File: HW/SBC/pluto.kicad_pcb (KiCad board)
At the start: 2 copper layers, 182.2 x 113 mm, 73 parts, among them J1 Serial Port, J2 VIA1PA, J3 VIA1PB, J4 BARREL_JACK, J6 AY-IO, J7 VIA2PB, P1 IDE0, Q1 DS1813, SW1 RESET, U1 WD65C02_, U10 74LS138, U11 LM7805CT, U12 WD65C22, U13 LM386, U14 AY-3-8912, U15 74LS74, U16 74LS32, U17 74LS139, U18 74HC74, U19 74LS08, U2 28C256, U20 74LS574, U21 74LS574, U22 74HC245, U3 AS6C62256A, U4 MAX232, U5 CDP65C51AE4, U6 WD65C22, U7 DS1511Y+, U8 74HCT00, U9 74LS30, X1 8 MHz

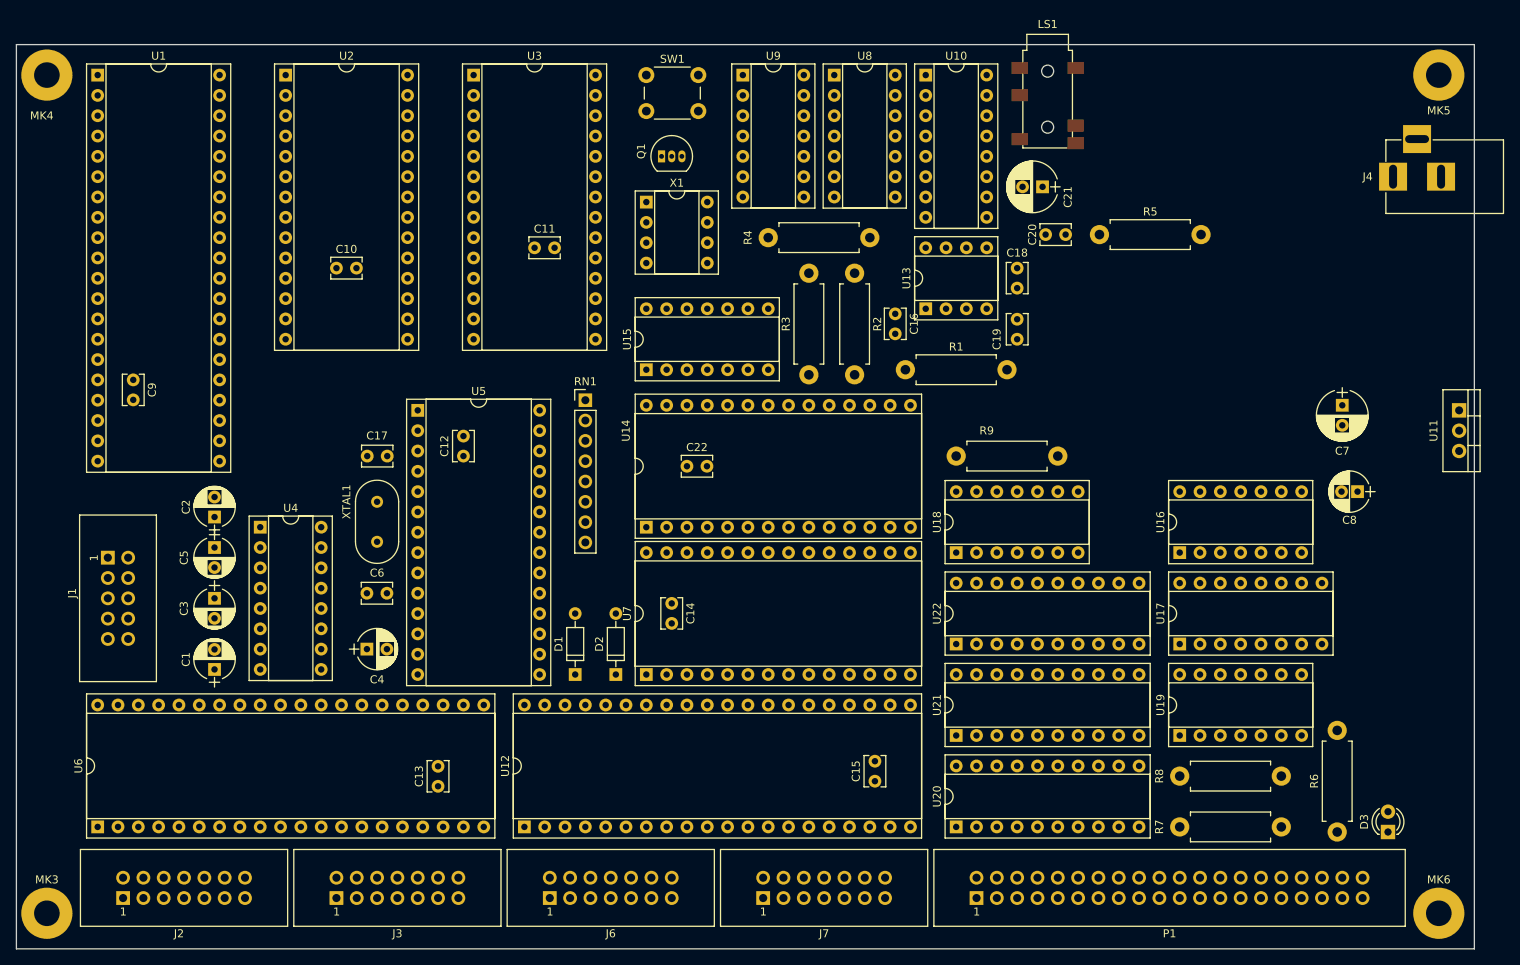
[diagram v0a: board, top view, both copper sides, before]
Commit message: Autorouted PCB.
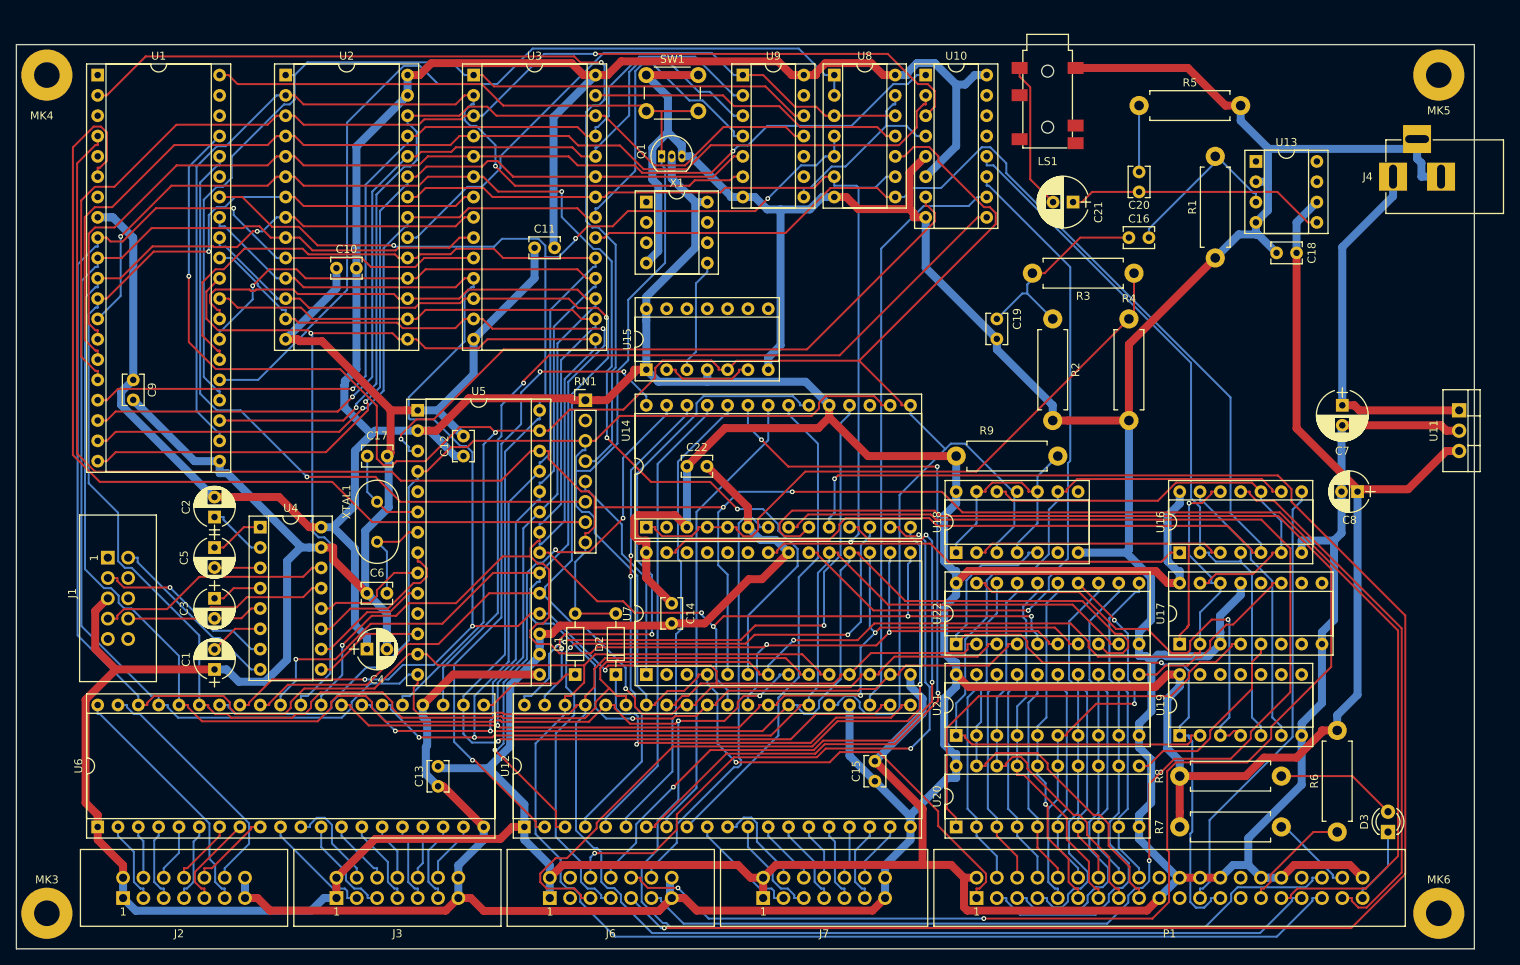
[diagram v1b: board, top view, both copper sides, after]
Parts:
- moved R4 46.2 mm to (165.1, 73.7), turned to 270 degrees
- moved U13 45.2 mm to (181.0, 54.0), turned to 0 degrees
- moved R3 42.6 mm to (165.7, 67.9), turned to 180 degrees
- moved R1 41.2 mm to (175.9, 66.0), turned to 90 degrees
- moved C18 35.0 mm to (186.1, 65.4), turned to 180 degrees
- moved C16 30.7 mm to (165.1, 63.5), turned to 0 degrees
- moved R2 25.4 mm to (155.6, 73.7)
- moved R5 16.9 mm to (166.4, 47.0)
- moved C20 12.8 mm to (166.4, 57.8), turned to 90 degrees
- moved C21 4.26 mm to (158.1, 59.1)
- moved C19 3.59 mm to (148.6, 73.7), turned to 270 degrees
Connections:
- net Net-(C7-Pad1) renamed +9V
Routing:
- net GND: track 0.00 -> 931.0 mm
- net VCC: track 0.00 -> 842.0 mm
- net /16bit IDE interface/A0: track 0.00 -> 342.0 mm, vias 0 -> 1
- net /16bit IDE interface/~RES: track 0.00 -> 329.5 mm, vias 0 -> 1
- net /16bit IDE interface/A1: track 0.00 -> 325.1 mm
- net /16bit IDE interface/A2: track 0.00 -> 311.5 mm, vias 0 -> 3
- net /16bit IDE interface/~IRQ: track 0.00 -> 307.6 mm, vias 0 -> 2
- net /16bit IDE interface/CLK: track 0.00 -> 293.4 mm, vias 0 -> 2
- net /16bit IDE interface/A3: track 0.00 -> 286.3 mm, vias 0 -> 3
- net /16bit IDE interface/D7: track 0.00 -> 248.0 mm, vias 0 -> 2
- net /16bit IDE interface/D6: track 0.00 -> 242.9 mm, vias 0 -> 3
- net /16bit IDE interface/D5: track 0.00 -> 226.0 mm, vias 0 -> 3
- net /16bit IDE interface/D3: track 0.00 -> 224.5 mm, vias 0 -> 5
- net /16bit IDE interface/D4: track 0.00 -> 219.5 mm, vias 0 -> 3
- net /Audio/IO_A4: track 0.00 -> 219.5 mm, vias 0 -> 2
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
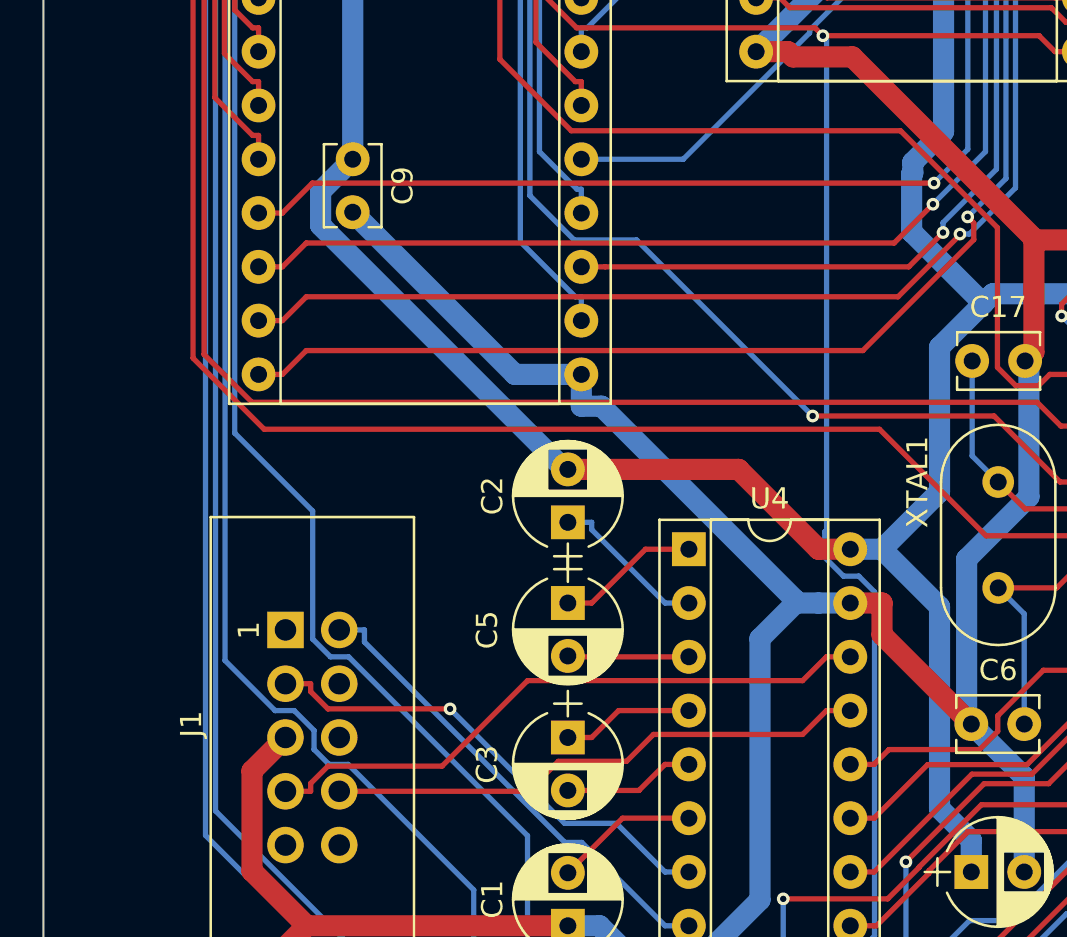
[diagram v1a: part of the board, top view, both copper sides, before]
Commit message: Added some silk screen text.
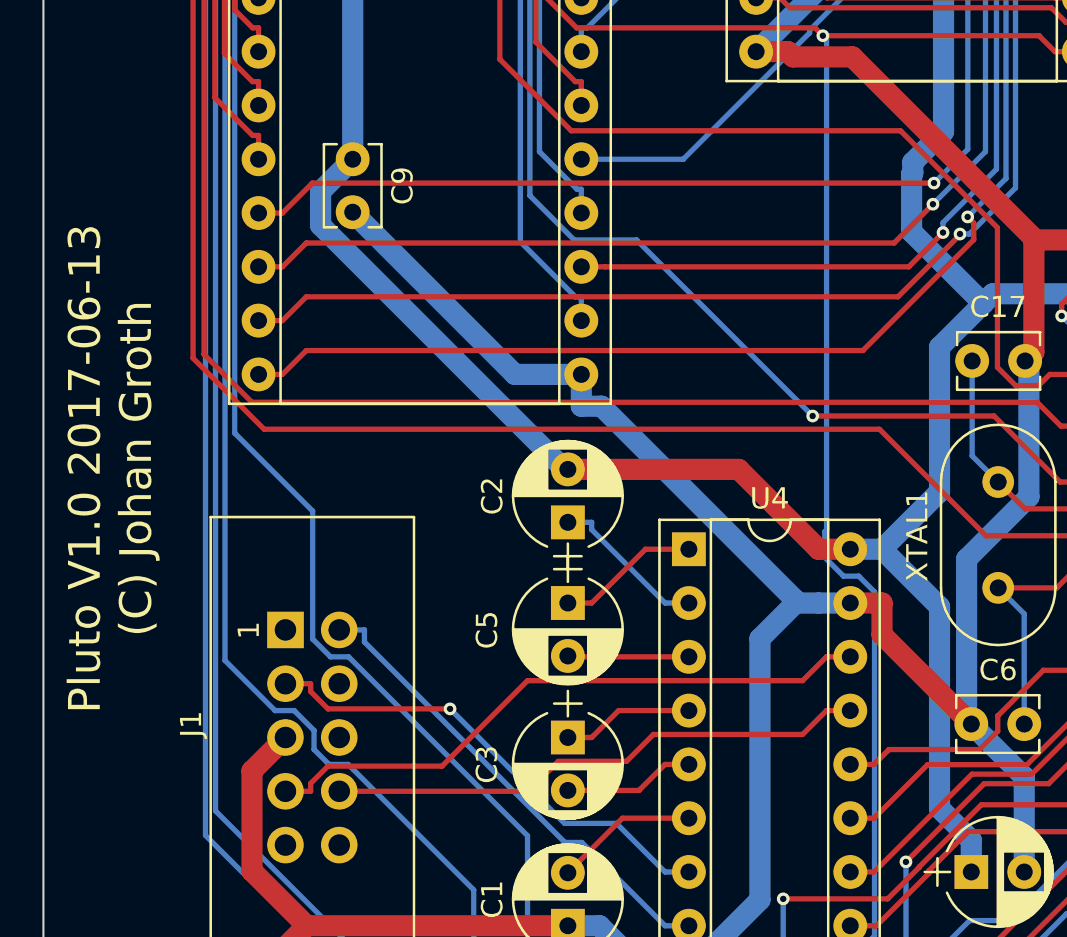
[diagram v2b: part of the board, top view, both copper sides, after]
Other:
- board text added: "Pluto V1.0 2017-06-13 (C) Johan Groth"
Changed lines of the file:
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@@
     (area 22.970238 34.820618 214.435 153.23)
     (thickness 1.6)
-    (drawings 4)
+    (drawings 5)
     (tracks 3039)
     (zones 0)
@@
       (outputformat 1)
       (mirror false)
-      (drillshape 1)
+      (drillshape 0)
       (scaleselection 1)
       (outputdirectory ""))
@@
     (descr "Ceramic Resomator/Filter 10.0x5.0 RedFrequency MG/MT/MX series, http://www.red-frequency.com/download/datenblatt/redfrequency-datenblatt-ir-zta.pdf, length*width=10.0x5.0mm^2 package, package length=10.0mm, package width=5.0mm, 2 pins")
     (tags "THT ceramic resonator filter")
-    (fp_text reference XTAL1 (at 0 3.81 270) (layer F.SilkS)
+    (fp_text reference XTAL1 (at 2.54 3.81 270) (layer F.SilkS)
       (effects (font (size 1 1) (thickness 0.15)))
     )
@@
     )
   )
+  (gr_text "Pluto V1.0 2017-06-13 \n(C) Johan Groth" (at 29.21 95.885 90) (layer F.SilkS)
+    (effects (font (size 1.5 1.5) (thickness 0.3)))
+  )
   (gr_line (start 26.035 152.4) (end 26.035 39.37) (angle 90) (layer Edge.Cuts) (width 0.1))
